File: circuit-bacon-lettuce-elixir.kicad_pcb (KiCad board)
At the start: 2 copper layers, 30 x 50 mm, 13 parts, among them J1 UART_MOD, J2 USB_CHG_DBG, J3 USB_DEV, SW1 RESET, U1 ESP32-C3-WROOM-02, U2 AP130-33Y

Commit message: feature: ロゴ・リポジトリURLを追加。
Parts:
- moved G*** 0.54 mm to (114.7, 119.2)
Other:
- board text added: "Bacon Lettuce Elixir"
- board text added: "https://github.com/ mecha-natori/ circuit-bacon- lettuce-elixir"

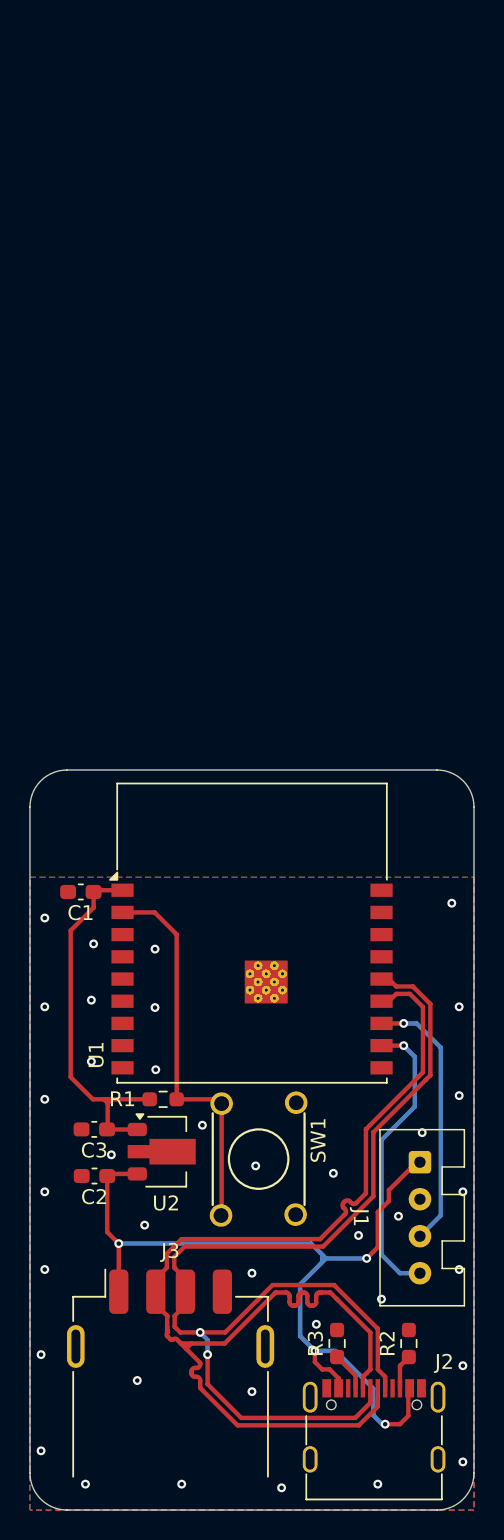
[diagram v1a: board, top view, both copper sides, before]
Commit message: feature: 書き込み・給電コネクタをType-CからType-Aへ変更。
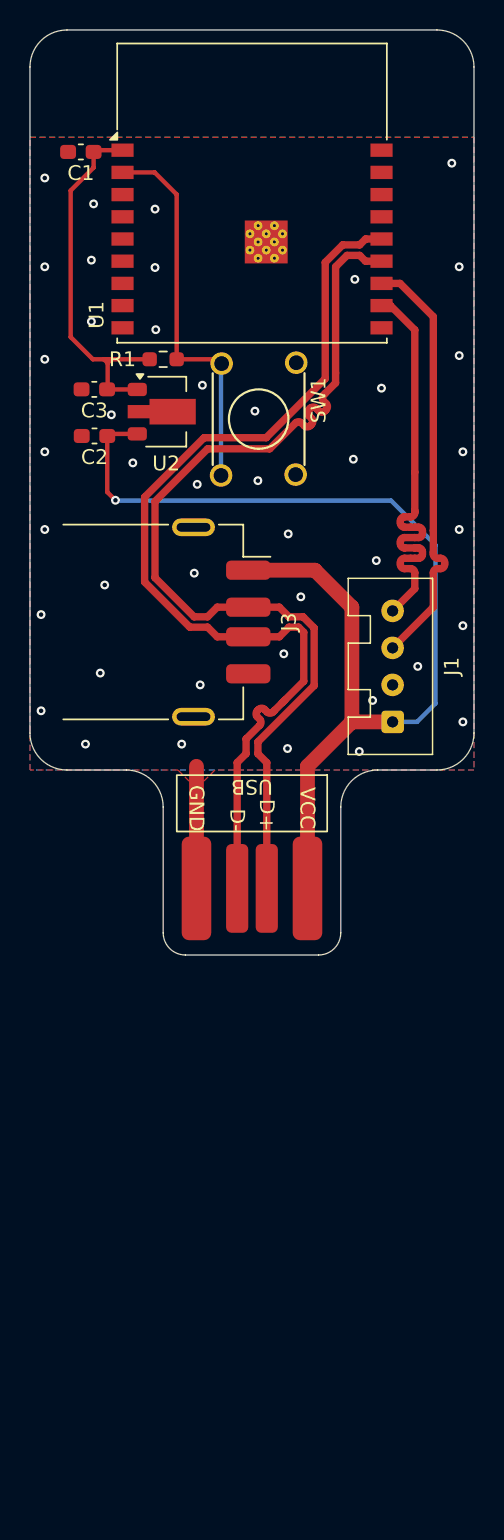
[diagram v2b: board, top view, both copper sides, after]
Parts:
- removed R2, R3: 5.1k, Resistor_SMD:R_0603_1608Metric_Pad0.98x0.95mm_HandSolder
- J2: footprint Connector_USB:USB_C_Receptacle_G-Switch_GT-USB-7010ASV -> circuit-bacon-lettuce-elixir:PCB_USB_Connecter
- moved J3 52.5 mm to (107.5, 90.0), turned to -90 degrees
- moved G*** 50.7 mm to (114.7, 68.6)
- moved C2 50.0 mm to (104.4, 77.4)
- moved C3 50.0 mm to (104.3, 74.3)
- moved R1 50.0 mm to (109.0, 72.2)
- moved SW1 50.0 mm to (115.5, 76.3)
- moved U1 50.0 mm to (115.0, 64.1)
- moved U2 50.0 mm to (109.2, 75.8)
- moved C1 50.0 mm to (103.4, 58.2)
- moved J2 38.4 mm to (115.0, 108.0), turned to -90 degrees
- moved J1 37.3 mm to (124.5, 93.0), turned to 90 degrees
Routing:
- net +5V: track 58.4 -> 74.7 mm, vias 4 -> 1
- net USB_N: track 82.5 -> 66.5 mm
- net Net-(J1-TX): track 18.0 -> 29.0 mm, vias 1 -> 0
- net USB_P: track 76.8 -> 66.5 mm, vias 2 -> 0
- net Net-(J1-RX): track 20.0 -> 28.9 mm, vias 1 -> 0
- net GND: track 0.00 -> 8.25 mm, vias 37 -> 43
- net Net-(J2-CC1): track 2.63 -> 0.00 mm
- net Net-(J2-CC2): track 2.36 -> 0.00 mm
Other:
- board size 30 x 50 mm -> 30 x 62.5 mm
- board text added: "Designed by @ms0503_"
